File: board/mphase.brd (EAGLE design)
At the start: 160 x 100 mm, 4 parts, among them IC1 MAX232, IC2 PIC18F4455_40, X1 332-10, X2 332-10

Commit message: updates
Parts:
- added C1, C2, C3, C4, C5, C6, C7: (no value), resistor:C025-025X050
- moved IC2 72.2 mm to (77.5, 40.6), turned to 270 degrees
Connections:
- new net N$1: C1.2, IC1.3
- new net N$10: IC1.10, IC2.29
- new net N$11: IC1.11, IC2.25
- new net N$12: IC1.12, IC2.26
- new net N$13: IC1.9, IC2.30
- new net N$2: C2.2, IC1.5
- new net N$3: C2.1, IC1.4
- new net N$4: C1.1, IC1.1
- new net N$5: C3.2, IC1.2
- new net N$6: C4.1, IC1.6
- new net N$9: C5.1, IC2.6
- net VDD: now also C6.1, C7.1
- net VSS: now also C3.1, C4.2, C7.2
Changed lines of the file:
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@@
 <layer number="97" name="Info" color="7" fill="1" visible="no" active="no"/>
 <layer number="98" name="Guide" color="6" fill="1" visible="no" active="no"/>
+<layer number="99" name="SpiceOrder" color="5" fill="1" visible="no" active="no"/>
 </layers>
 <board>
@@
 <element name="X1" library="con-garry" package="332-10" value="332-10" x="97.79" y="78.74"/>
 <element name="X2" library="con-garry" package="332-10" value="332-10" x="57.15" y="77.47"/>
-<element name="IC2" library="microchip" package="DIL40" value="PIC18F4455_40" x="31.75" y="-15.24">
-<attribute name="OC_FARNELL" value="9321314" x="31.75" y="-15.24" size="1.778" layer="27" display="off"/>
-<attribute name="OC_NEWARK" value="05K2028" x="31.75" y="-15.24" size="1.778" layer="27" display="off"/>
-<attribute name="MF" value="MICROCHIP" x="31.75" y="-15.24" size="1.778" layer="27" display="off"/>
-<attribute name="MPN" value="PIC18F4455-I/P" x="31.75" y="-15.24" size="1.778" layer="27" display="off"/>
+<element name="IC2" library="microchip" package="DIL40" value="PIC18F4455_40" x="77.47" y="40.64" rot="R270">
+<attribute name="OC_FARNELL" value="9321314" x="77.47" y="40.64" size="1.778" layer="27" rot="R270" display="off"/>
+<attribute name="OC_NEWARK" value="05K2028" x="77.47" y="40.64" size="1.778" layer="27" rot="R270" display="off"/>
+<attribute name="MF" value="MICROCHIP" x="77.47" y="40.64" size="1.778" layer="27" rot="R270" display="off"/>
+<attribute name="MPN" value="PIC18F4455-I/P" x="77.47" y="40.64" size="1.778" layer="27" rot="R270" display="off"/>
 </element>
+<element name="C1" library="resistor" package="C025-025X050" value="" x="8.89" y="-7.62"/>
+<element name="C2" library="resistor" package="C025-025X050" value="" x="8.89" y="-21.59"/>
+<element name="C3" library="resistor" package="C025-025X050" value="" x="8.89" y="-35.56"/>
+<element name="C4" library="resistor" package="C025-025X050" value="" x="8.89" y="-49.53"/>
+<element name="C5" library="resistor" package="C025-025X050" value="" x="8.89" y="-63.5"/>
+<element name="C6" library="resistor" package="C025-025X050" value="" x="8.89" y="-77.47"/>
+<element name="C7" library="resistor" package="C025-025X050" value="" x="8.89" y="-91.44"/>
 </elements>
 <signals>
@@
 <contactref element="IC2" pad="12"/>
 <contactref element="IC2" pad="31"/>
-<wire x1="35.56" y1="-22.86" x2="30.48" y2="-7.62" width="0" layer="19" extent="1-1"/>
+<contactref element="C4" pad="2"/>
+<contactref element="C3" pad="1"/>
+<contactref element="C7" pad="2"/>
+<wire x1="69.85" y1="36.83" x2="85.09" y2="41.91" width="0" layer="19" extent="1-1"/>
+<wire x1="7.62" y1="-35.56" x2="69.85" y2="36.83" width="0" layer="19" extent="1-1"/>
+<wire x1="10.16" y1="-49.53" x2="7.62" y2="-35.56" width="0" layer="19" extent="1-1"/>
+<wire x1="10.16" y1="-91.44" x2="10.16" y2="-49.53" width="0" layer="19" extent="1-1"/>
+</signal>
+<signal name="N$1">
+<contactref element="C1" pad="2"/>
+<contactref element="IC1" pad="3"/>
+<wire x1="10.16" y1="-7.62" x2="76.2" y2="86.36" width="0" layer="19" extent="1-1"/>
+</signal>
+<signal name="N$2">
+<contactref element="C2" pad="2"/>
+<contactref element="IC1" pad="5"/>
+<wire x1="10.16" y1="-21.59" x2="81.28" y2="86.36" width="0" layer="19" extent="1-1"/>
+</signal>
+<signal name="N$3">
+<contactref element="C2" pad="1"/>
+<contactref element="IC1" pad="4"/>
+<wire x1="7.62" y1="-21.59" x2="78.74" y2="86.36" width="0" layer="19" extent="1-1"/>
+</signal>
+<signal name="N$4">
+<contactref element="C1" pad="1"/>
+<contactref element="IC1" pad="1"/>
+<wire x1="7.62" y1="-7.62" x2="71.12" y2="86.36" width="0" layer="19" extent="1-1"/>
+</signal>
+<signal name="N$5">
+<contactref element="IC1" pad="2"/>
+<contactref element="C3" pad="2"/>
+<wire x1="10.16" y1="-35.56" x2="73.66" y2="86.36" width="0" layer="19" extent="1-1"/>
+</signal>
+<signal name="N$6">
+<contactref element="IC1" pad="6"/>
+<contactref element="C4" pad="1"/>
+<wire x1="7.62" y1="-49.53" x2="83.82" y2="86.36" width="0" layer="19" extent="1-1"/>
+</signal>
+<signal name="N$9">
+<contactref element="IC2" pad="6"/>
+<contactref element="C5" pad="1"/>
+<wire x1="7.62" y1="-63.5" x2="69.85" y2="52.07" width="0" layer="19" extent="1-1"/>
+</signal>
+<signal name="N$10">
+<contactref element="IC2" pad="29"/>
+<contactref element="IC1" pad="10"/>
+<wire x1="85.09" y1="36.83" x2="86.36" y2="93.98" width="0" layer="19" extent="1-1"/>
+</signal>
+<signal name="N$11">
+<contactref element="IC2" pad="25"/>
+<contactref element="IC1" pad="11"/>
+<wire x1="85.09" y1="26.67" x2="83.82" y2="93.98" width="0" layer="19" extent="1-1"/>
+</signal>
+<signal name="N$12">
+<contactref element="IC2" pad="26"/>
+<contactref element="IC1" pad="12"/>
+<wire x1="85.09" y1="29.21" x2="81.28" y2="93.98" width="0" layer="19" extent="1-1"/>
+</signal>
+<signal name="N$13">
+<contactref element="IC2" pad="30"/>
+<contactref element="IC1" pad="9"/>
+<wire x1="85.09" y1="39.37" x2="88.9" y2="93.98" width="0" layer="19" extent="1-1"/>
 </signal>
 <signal name="VDD">
+<contactref element="C6" pad="1"/>
 <contactref element="IC2" pad="11"/>
+<contactref element="C7" pad="1"/>
 <contactref element="IC2" pad="32"/>
-<wire x1="33.02" y1="-22.86" x2="27.94" y2="-7.62" width="0" layer="19" extent="1-1"/>
+<wire x1="69.85" y1="39.37" x2="85.09" y2="44.45" width="0" layer="19" extent="1-1"/>
+<wire x1="7.62" y1="-77.47" x2="69.85" y2="39.37" width="0" layer="19" extent="1-1"/>
+<wire x1="7.62" y1="-91.44" x2="7.62" y2="-77.47" width="0" layer="19" extent="1-1"/>
 </signal>
 </signals>

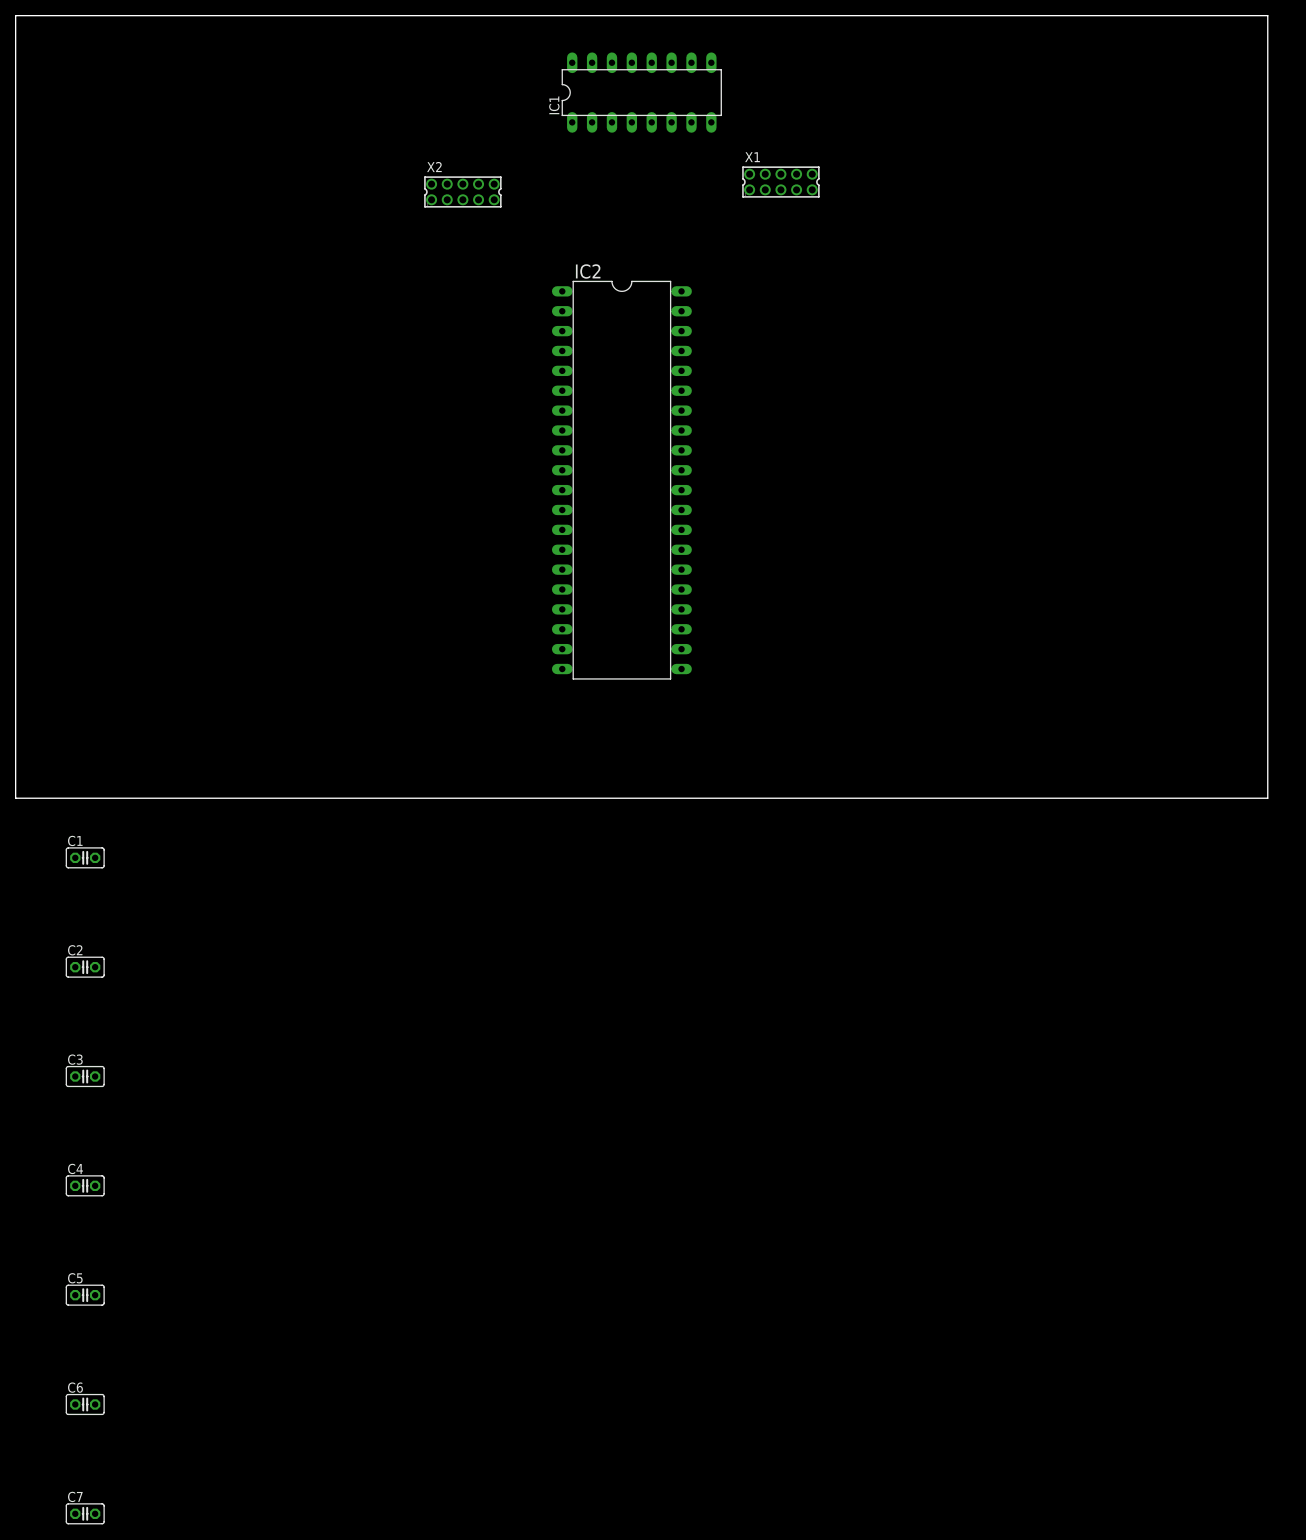
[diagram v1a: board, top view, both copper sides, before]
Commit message: 
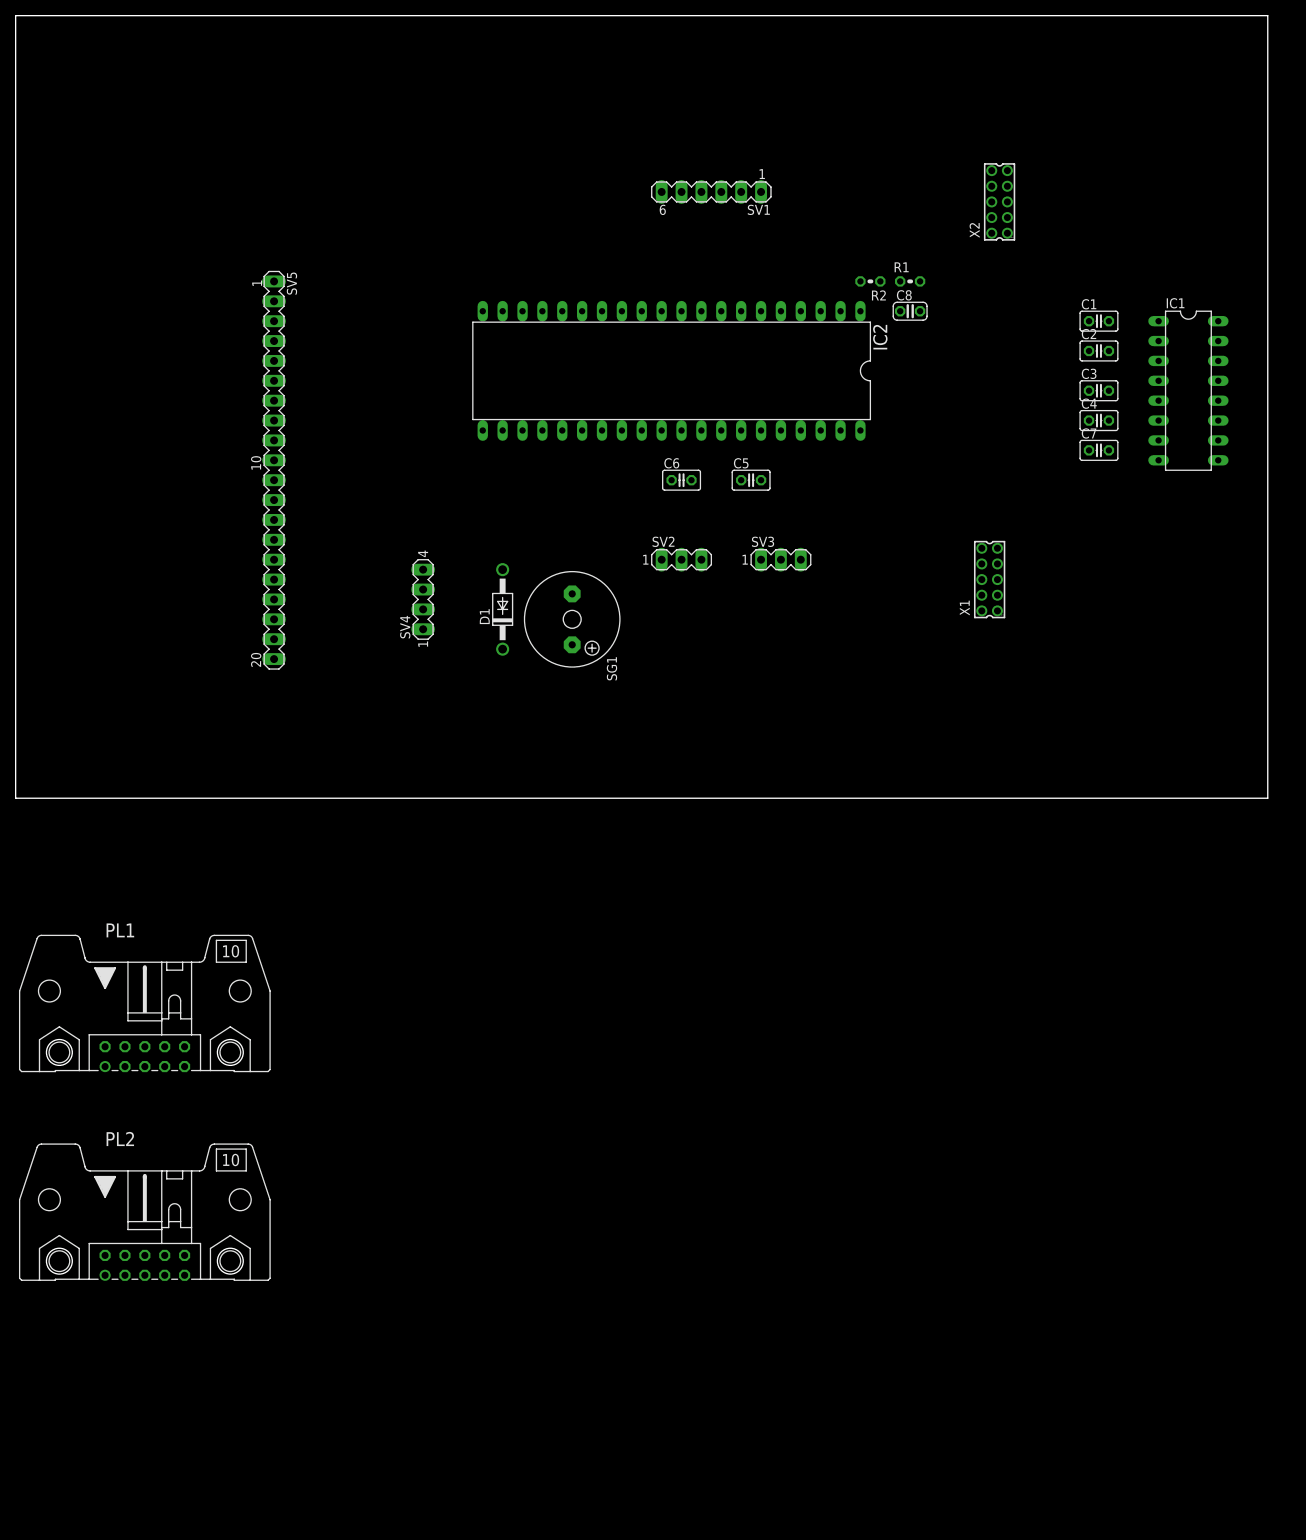
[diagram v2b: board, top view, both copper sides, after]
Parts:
- added C8: 0.1, resistor:C025-024X044
- added D1: 1N4004, diode:DO41-10
- added PL1, PL2: (no value), con-harting-h:10H
- added R1: 10000, resistor:0204V
- added R2: 220, resistor:0204V
- added SG1: F/QMX, buzzer:F/QMX
- added SV1: (no value), con-lstb:MA06-1
- added SV2, SV3: (no value), con-lstb:MA03-1
- added SV4: (no value), con-lstb:MA04-1
- added SV5: (no value), con-lstb:MA20-1
- C1, C2, C3, C4: value (none) -> 1uf
- C5: value (none) -> 3.3uf
- C6: value (none) -> 0.1
- C7: value (none) -> 22uf
- moved C7 187.7 mm to (138.4, 44.5)
- moved C4 162.3 mm to (138.4, 48.3)
- moved C3 156.4 mm to (138.4, 52.1)
- moved C2 151.6 mm to (138.4, 57.1)
- moved C1 146.6 mm to (138.4, 61.0)
- moved C6 140.6 mm to (85.1, 40.6)
- moved C5 134.5 mm to (94.0, 40.6)
- moved IC1 79.6 mm to (149.9, 52.1), turned to 270 degrees
- moved X2 68.6 mm to (125.7, 76.2), turned to 90 degrees
- moved X1 57.4 mm to (124.5, 27.9), turned to 90 degrees
- moved IC2 15.3 mm to (83.8, 54.6), turned to 180 degrees
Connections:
- new net N$14: IC2.1, R2.2
- new net N$15: IC1.8, X2.4
- new net N$16: IC1.7, X2.6
- new net N$17: X1.4, X1.6
- new net N$18: X1.1, X1.2, X1.7
- new net N$19: IC1.14, X1.3
- new net N$20: IC1.13, X1.5
- new net N$7: D1.A, IC2.7, SG1.-
- new net N$8: C8.1, R1.2, R2.1
- net GND: now also C8.2, X1.9, X2.10
- net VCC: now also C6.1, IC2.11
- net VDD: now also D1.C, R1.1, SG1.+, X2.1; no longer C6.1, IC2.11
- net VSS: now also C5.2, C6.2

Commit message: update code
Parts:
- removed R2: 220, resistor:0204V
- added C10, C9: 0.1, resistor:C025-024X044
- added C11: 22uf, resistor:C025-025X050
- added D2: BZX55, diode:DO35Z10
- added R3, R5, R6: 220, resistor:0204V
- added R4, R7: 10000, resistor:0204V
- moved PL1 171.8 mm to (144.8, 81.3), turned to 270 degrees
- moved PL2 152.5 mm to (144.8, 22.9), turned to 270 degrees
- moved C3 14.0 mm to (124.5, 53.3)
- moved C4 14.0 mm to (124.5, 49.5)
- moved C7 14.0 mm to (124.5, 45.7)
- moved IC1 14.0 mm to (135.9, 52.1)
- moved C1 14.0 mm to (124.5, 61.0)
- moved C2 14.0 mm to (124.5, 57.1)
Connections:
- removed net N$15: IC1.8, X2.4
- removed net N$18: X1.1, X1.2, X1.7
- new net N$21: C9.1, IC2.34, R4.2, R6.1
- new net N$22: C10.1, IC2.33, R5.2, R7.1
- new net N$24: R6.2, SV2.2
- new net N$25: R5.1, SV2.3
- net GND: now also PL1.10, PL2.9
- net N$14: now also R3.2; no longer R2.2
- net N$16: now also PL1.6
- net N$17: now also IC1.8, PL1.4, X2.4; no longer X1.4, X1.6
- net N$19: now also PL2.3
- net N$20: now also PL2.5
- net N$8: now also R3.1; no longer R2.1
- net VDD: now also C11.1, D2.C, PL1.1, R4.1, R7.2, SV4.3
- net VSS: now also C10.2, C11.2, C9.2, D2.A, SV2.1, SV3.1, SV4.1
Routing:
- net VDD: track 0.00 -> 197.7 mm
- net VSS: track 0.00 -> 158.6 mm, vias 0 -> 1
- net GND: track 0.00 -> 145.3 mm, vias 0 -> 1
- net N$12: track 0.00 -> 119.6 mm
- net N$11: track 0.00 -> 109.3 mm
- net VCC: track 0.00 -> 97.0 mm, vias 0 -> 1
- net N$10: track 0.00 -> 90.6 mm
- net N$13: track 0.00 -> 88.9 mm
- net N$17: track 0.00 -> 83.4 mm, vias 0 -> 1
- net N$16: track 0.00 -> 68.5 mm, vias 0 -> 1
- net N$7: track 0.00 -> 54.2 mm
- net N$8: track 0.00 -> 50.7 mm
- net N$19: track 0.00 -> 48.1 mm
- net N$20: track 0.00 -> 47.9 mm
- net N$22: track 0.00 -> 46.4 mm
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
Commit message: updates
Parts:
- added C12: 0.1, resistor:C025-024X044
- added LED1: TLLR4400, led:LED3MM
- added R2, R9: 220, resistor:0204V
- added R8: 10000, resistor:0204V
- moved PL1 58.6 mm to (88.9, 63.5)
- moved PL2 56.0 mm to (88.9, 19.1)
- moved C8 53.7 mm to (61.0, 68.6)
- moved R1 53.7 mm to (61.0, 72.4)
- moved X2 52.8 mm to (78.7, 52.1)
- moved C10 48.3 mm to (59.7, 43.2)
- moved C9 47.1 mm to (54.6, 43.2)
- moved X1 45.8 mm to (78.7, 30.5)
- moved IC2 45.8 mm to (38.1, 57.1)
- moved C5 44.5 mm to (49.5, 43.2)
- moved C6 42.0 mm to (43.2, 43.2)
- moved R3 39.7 mm to (68.6, 24.1)
- moved R5 39.7 mm to (68.6, 27.9)
- moved R7 39.7 mm to (68.6, 31.8)
- moved R4 39.6 mm to (68.6, 35.6)
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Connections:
- new net N$15: IC2.2, R2.2, SV5.1
- new net N$18: LED1.A, R2.1
- new net N$23: IC2.3, SV5.2
- new net N$26: IC2.4, SV5.3
- new net N$27: IC2.5, SV5.4
- new net N$28: C12.1, IC2.35, R8.1, R9.1
- new net N$29: IC2.40, SV1.4
- new net N$30: IC2.14, SV5.11
- new net N$31: R9.2, SV3.3
- new net N$32: IC2.39, SV1.5
- new net N$33: IC2.16, SV3.1
- new net N$34: IC2.17, SV3.2
- net N$8: now also SV1.1, SV5.19
- net VDD: now also R8.2, SV1.2
- net VSS: now also C12.2, LED1.K, SV1.3, SV5.20; no longer SV3.1
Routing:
- net N$34: track 0.00 -> 82.0 mm
- net N$8: track 50.7 -> 125.1 mm
- net VSS: track 158.6 -> 224.9 mm
- net N$15: track 0.00 -> 57.6 mm
- net N$33: track 0.00 -> 54.5 mm, vias 0 -> 1
- net N$23: track 0.00 -> 53.1 mm
- net N$26: track 0.00 -> 51.9 mm
- net N$27: track 0.00 -> 47.9 mm
- net N$32: track 0.00 -> 38.4 mm, vias 0 -> 1
- net VCC: track 97.0 -> 132.5 mm, vias 1 -> 0
- net N$30: track 0.00 -> 34.5 mm
- net N$29: track 0.00 -> 30.5 mm
- net N$31: track 0.00 -> 28.1 mm
- net N$13: track 88.9 -> 112.3 mm
- net GND: track 145.3 -> 122.5 mm
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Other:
- board size 160 x 100 mm -> 120.6 x 82.2 mm

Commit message: update board
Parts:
- added C13: 0.1, resistor:C025-024X044
- added C14: 22uf, resistor:C025-025X050
- added C15: 0.1, resistor:C025-025X050
- added JMP1: 0R-JUMPA, jump-0r-smd:A0R-JMP
- moved C7 65.4 mm to (35.6, 71.1)
- moved IC1 47.2 mm to (74.9, 68.6)
- moved C1 45.0 mm to (67.3, 66.0), turned to 270 degrees
- moved C3 43.3 mm to (67.3, 73.7), turned to 90 degrees
- moved C4 36.6 mm to (67.3, 57.1), turned to 90 degrees
- moved C2 34.9 mm to (82.5, 69.8), turned to 270 degrees
- moved X2 9.25 mm to (76.2, 43.2)
- moved PL2 7.62 mm to (88.9, 26.7)
- moved SV1 7.62 mm to (49.5, 77.5)
- moved R1 5.68 mm to (63.5, 77.5)
- moved R8 5.24 mm to (41.9, 36.8)
- moved R9 4.02 mm to (35.6, 36.8)
- moved R3 3.81 mm to (68.6, 20.3)
- moved R2 3.81 mm to (44.5, 71.1)
- moved LED1 2.84 mm to (50.8, 69.8)
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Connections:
- net GND: now also C14.2, C15.2
- net VCC: now also C14.1, C15.1, JMP1.1; no longer C6.1, IC2.11
- net VDD: now also C13.1, C6.1, IC2.11, JMP1.3
- net VSS: now also C13.2
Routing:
- net VCC: track 132.5 -> 35.3 mm
- net N$13: track 112.3 -> 49.3 mm, vias 0 -> 3
- net N$12: track 121.0 -> 61.8 mm, vias 0 -> 1
- net N$17: track 82.2 -> 42.0 mm
- net VSS: track 224.9 -> 186.0 mm, vias 1 -> 0
- net VDD: track 195.9 -> 224.2 mm, vias 0 -> 1
- net N$10: track 107.8 -> 81.1 mm, vias 1 -> 0
- net N$11: track 120.3 -> 94.0 mm
- net N$33: track 54.5 -> 75.9 mm
- net N$34: track 82.0 -> 60.9 mm
- net N$16: track 63.1 -> 45.4 mm
- net N$20: track 57.5 -> 75.2 mm
- net N$19: track 49.5 -> 67.0 mm
- net N$8: track 125.1 -> 138.9 mm
- net N$5: track 15.3 -> 3.85 mm
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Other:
- board size 120.6 x 82.2 mm -> 111.7 x 74.6 mm
- board text added: "FGB@MCHP"
- board text added: "MPHASE 1.0"

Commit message: update board
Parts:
- IC2: value PIC18F4455_40 -> PIC18F45K80
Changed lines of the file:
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@@
 <?xml version="1.0" encoding="utf-8"?>
 <!DOCTYPE eagle SYSTEM "eagle.dtd">
-<eagle version="9.5.0">
+<eagle version="9.6.2">
 <drawing>
 <settings>
@@
 <attribute name="VALUE" x="73.66" y="44.91" size="1.27" layer="27" rot="R90"/>
 </element>
-<element name="IC2" library="microchip" package="DIL40" value="PIC18F4455_40" x="38.1" y="57.15" smashed="yes" rot="R180">
+<element name="IC2" library="microchip" package="DIL40" value="PIC18F45K80" x="38.1" y="57.15" smashed="yes" rot="R180">
 <attribute name="MF" value="MICROCHIP" x="38.1" y="57.15" size="1.778" layer="27" rot="R180" display="off"/>
 <attribute name="MPN" value="PIC18F45K80" x="38.1" y="57.15" size="1.778" layer="27" rot="R180" display="off"/>
